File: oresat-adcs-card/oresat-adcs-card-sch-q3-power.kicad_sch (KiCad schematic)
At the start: 87 parts, among them Q31 MOSFET-PCH-SOT23-6, Q32 MOSFET-PCH-SOT23-6, Q33 PMV45EN2R, Q34 PMV45EN2R, Q35 MOSFET-PCH-dual-SOT23-6, U25 MAX7310ATE, U26 MAX4211FETE, U27 MIC842LYC5-TR, U28 MIC842LYC5-TR, U35 LTC3624, U37 TS5A21366DCUR

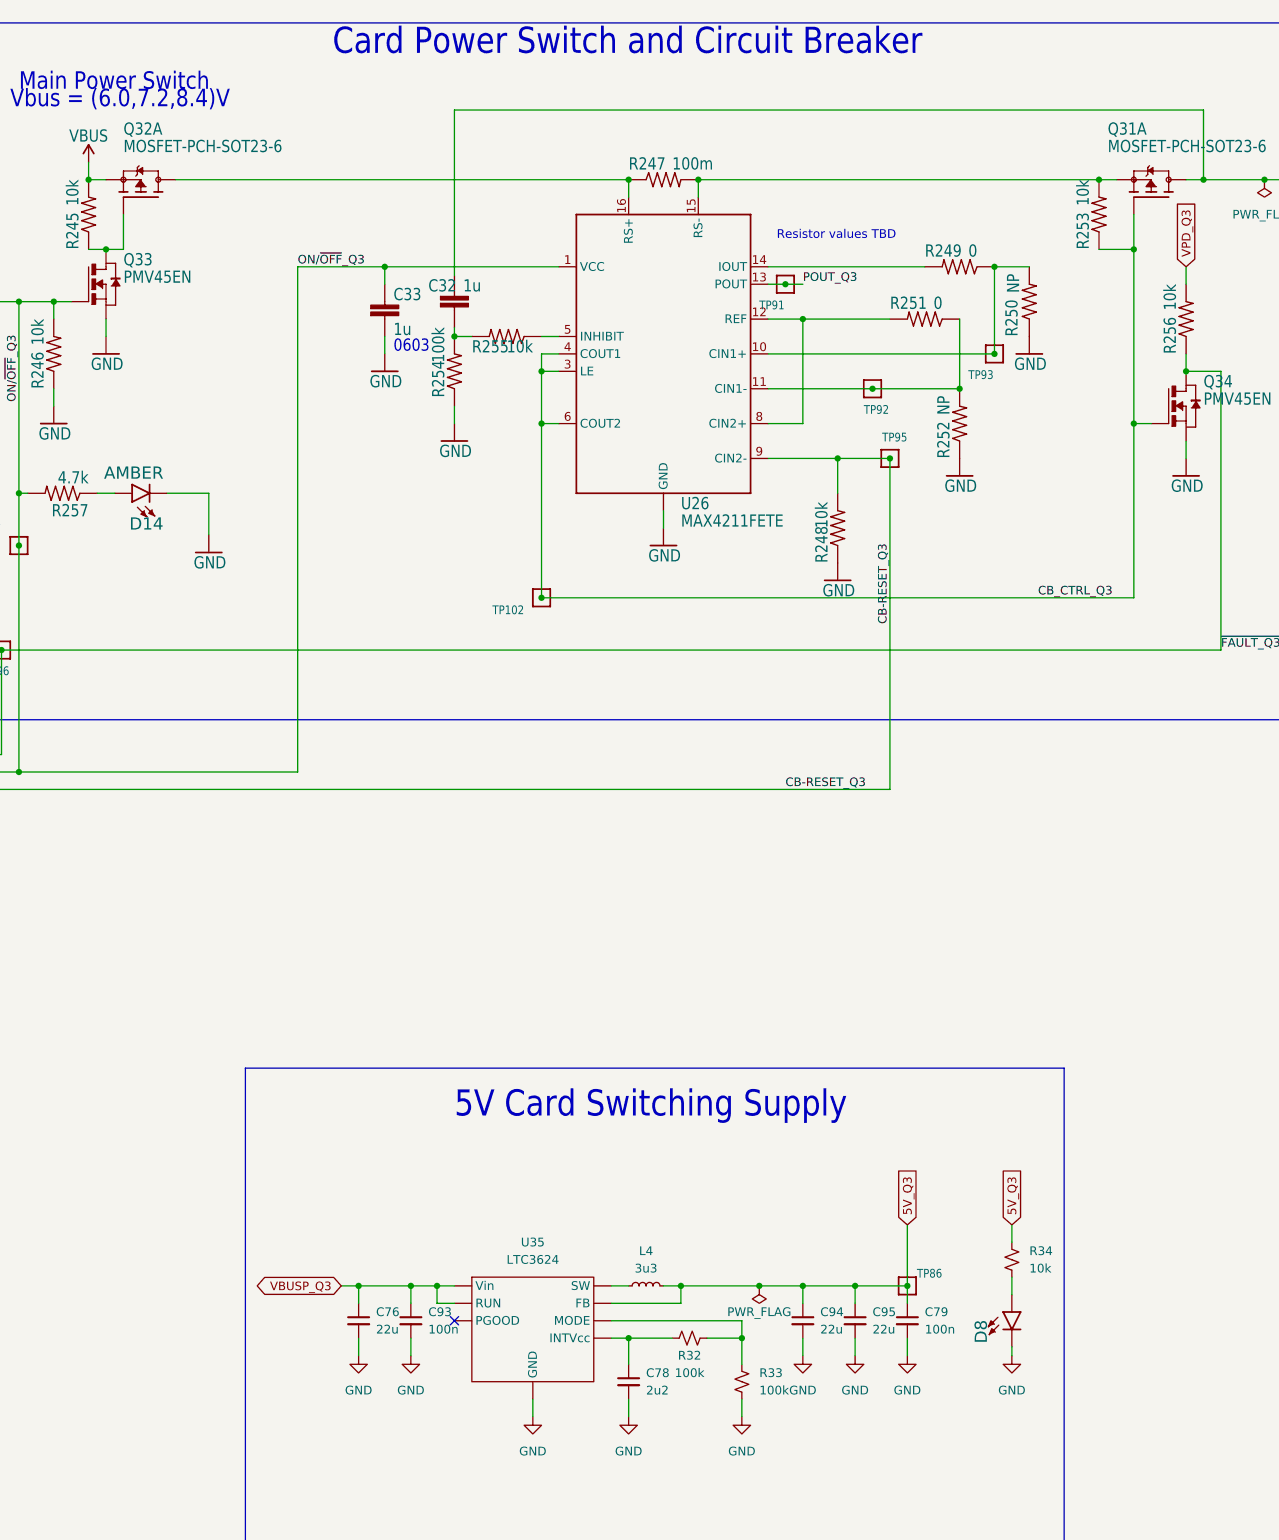
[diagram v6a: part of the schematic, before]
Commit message: Updated ADCS card and fixed library issues
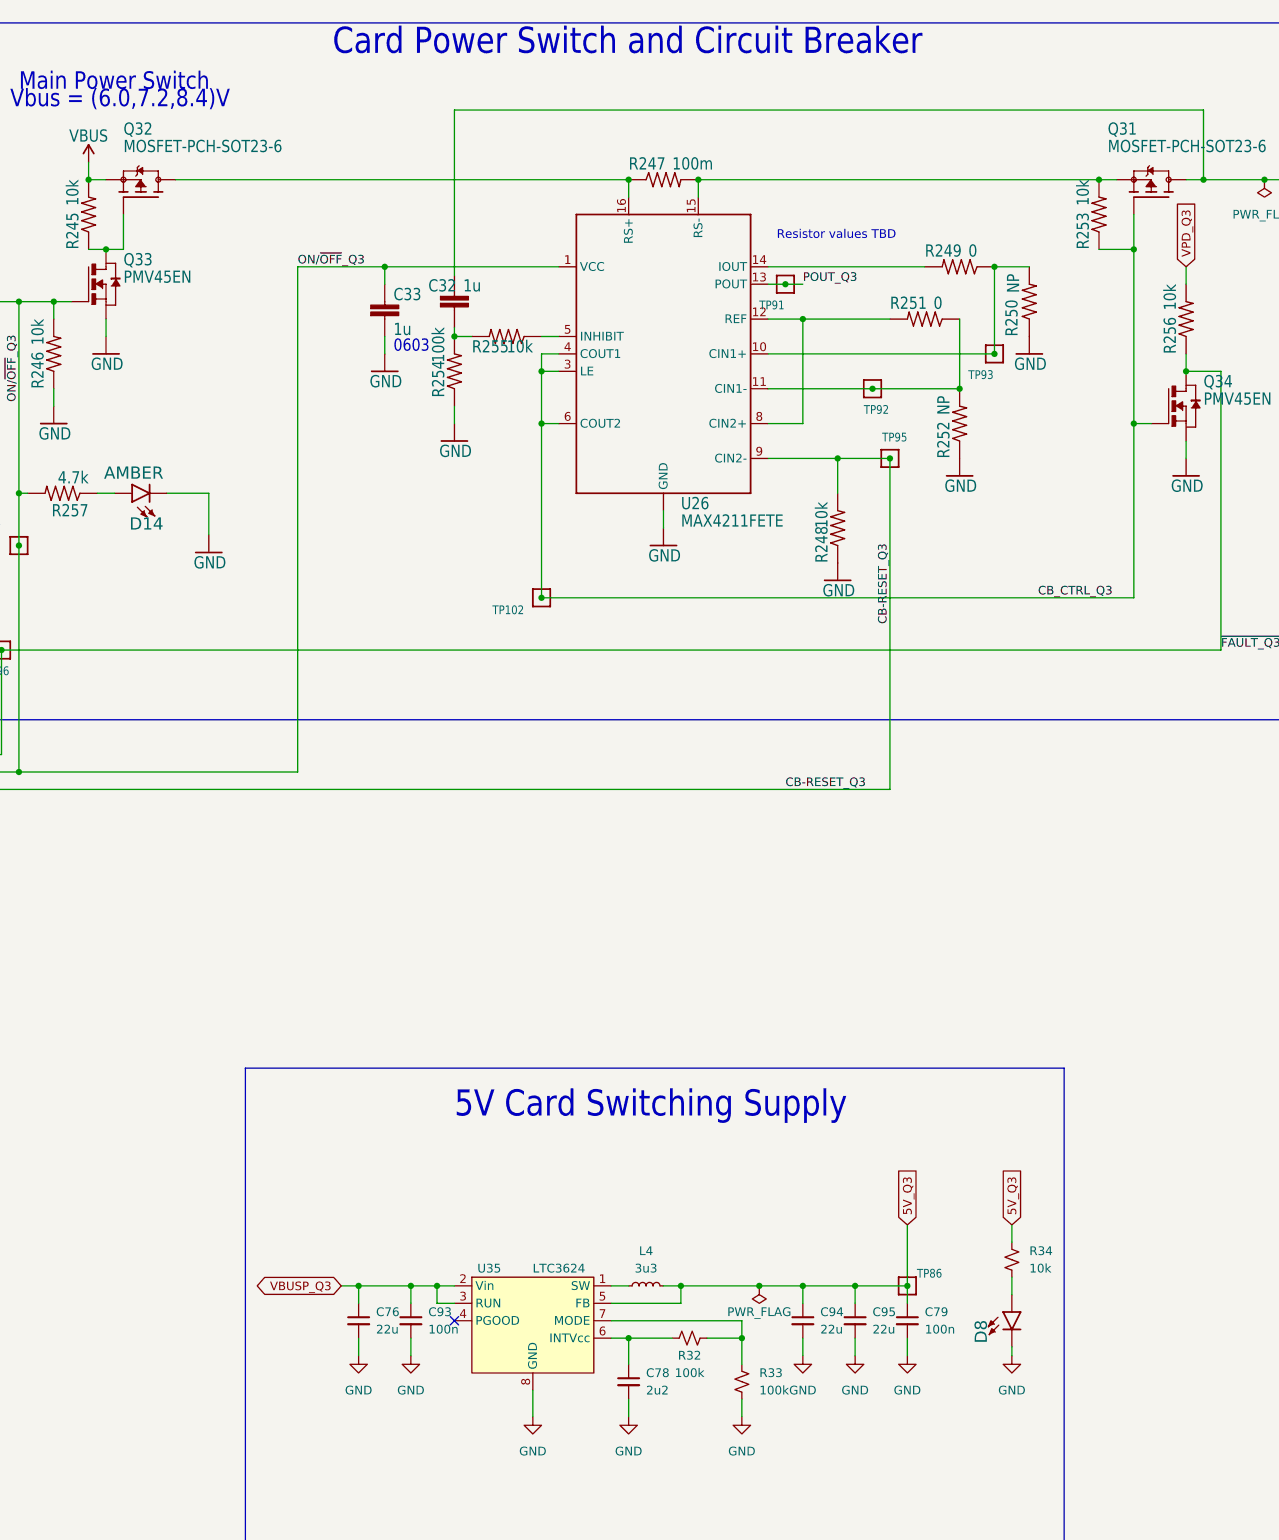
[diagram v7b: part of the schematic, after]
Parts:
- C31, C32, C33, C34, C35, C83, R115, R127, R229, R230, R231, R232, R233, R234, R235, R236, R237, R238, R239, R240, R241, R242, R243, R244, R245, R246, R248, R249, R250, R251, R252, R253, R254, R255, R256, R257, R258, R259, R260, R261, R262, R263, R264, R265, R266, R38: footprint oresat-acs-card:.0603-C-NOSILK -> oresat-passives:0603-C-NOSILK
- L4: footprint oresat-footprints:L_ECS-MPI4040 -> oresat-passives:L_ECS-MPI4040
- U35: footprint oresat-footprints:DFN-8-1EP_3x3mm_P0.5mm_EP1.65x2.38mm_ThermalVias0.3mm -> oresat-ics:DFN-8-1EP_3x3mm_P0.5mm_EP1.65x2.38mm_ThermalVias0.3mm; symbol U-Linear Tech-LTC3624:LTC3624 -> oresat-ics:LTC3624

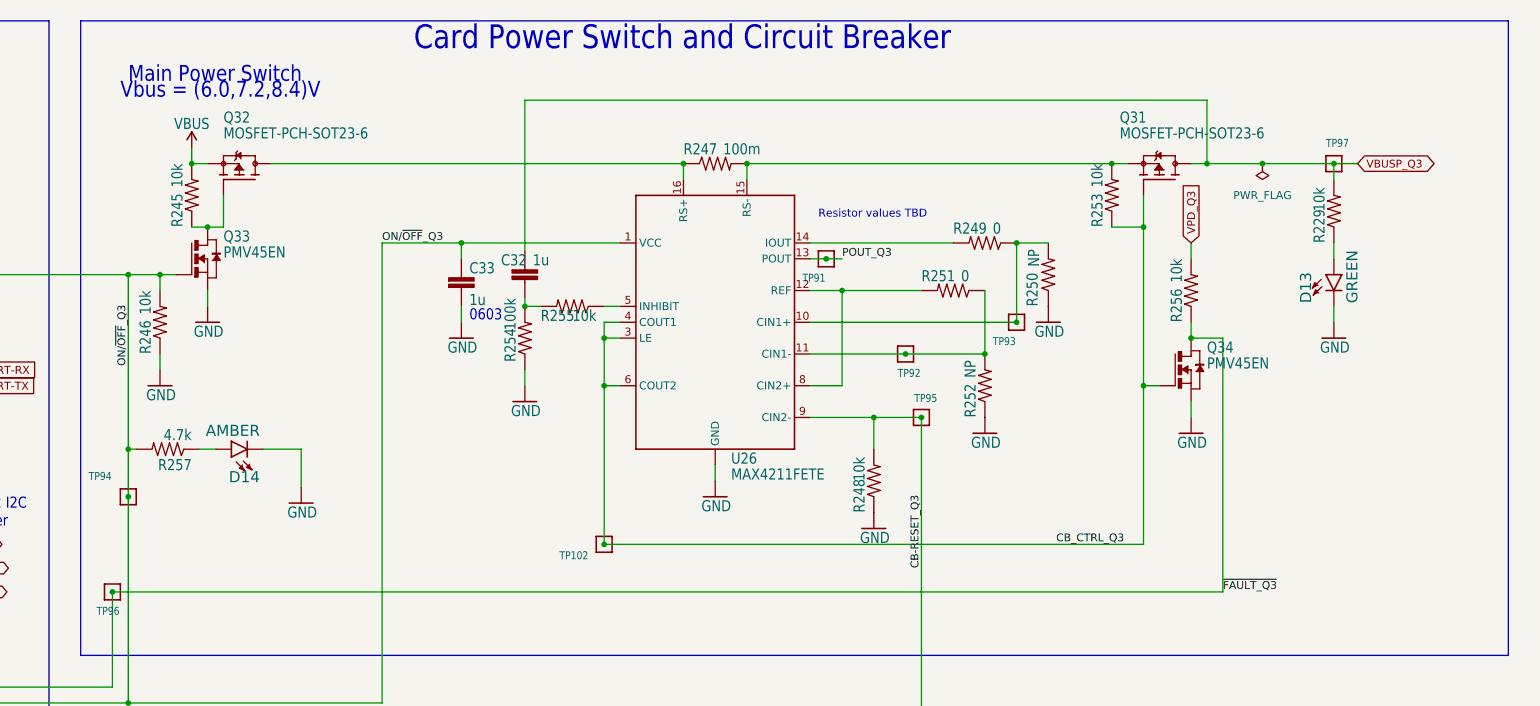
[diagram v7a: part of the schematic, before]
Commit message: Updated ADCS card, added soft-start to RW OPDs and updated current limits
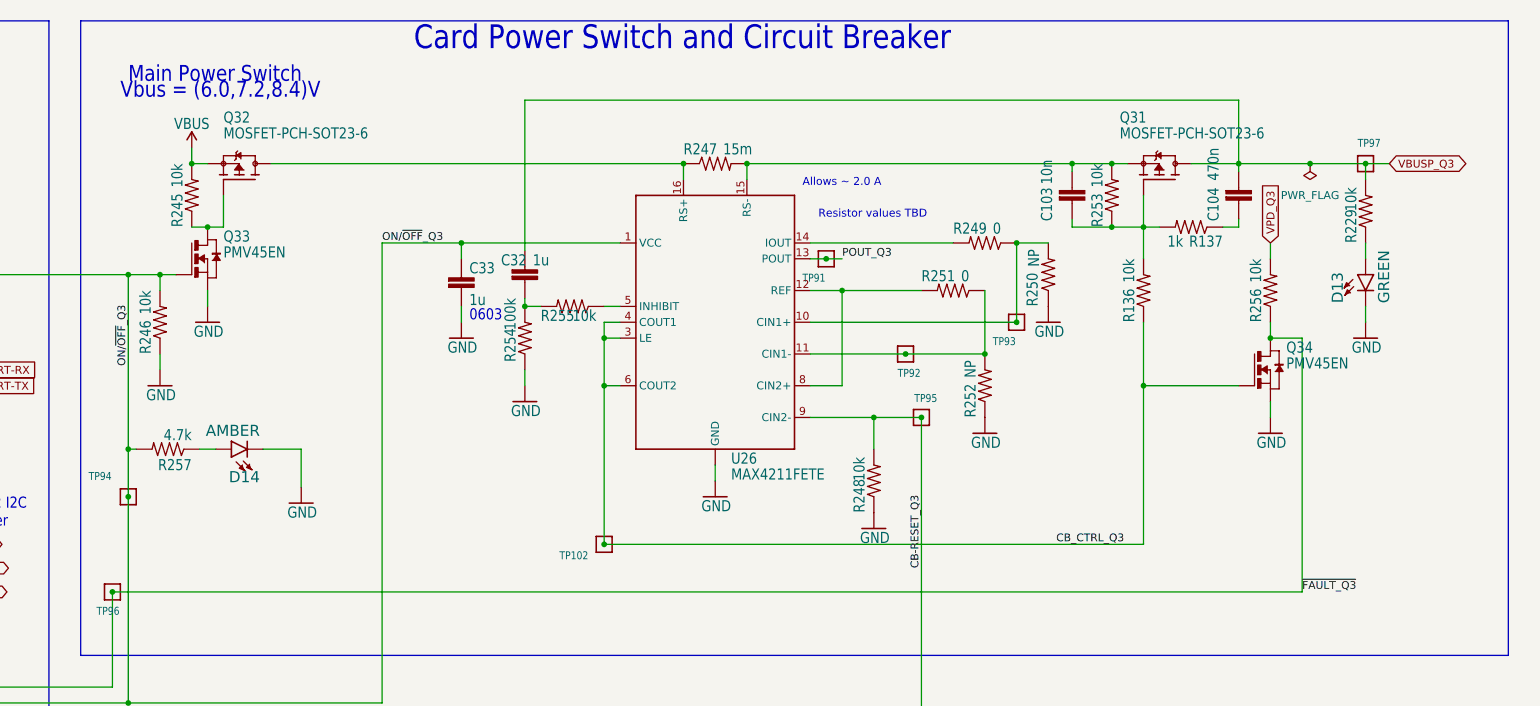
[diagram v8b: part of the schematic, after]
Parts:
- added C103: 10n, oresat-passives:0603-C-NOSILK, symbol oresat-acs-card-eagle-import:C-EU0603-C-NOSILK
- added C104: 470n, oresat-passives:0603-C-NOSILK, symbol oresat-acs-card-eagle-import:C-EU0603-C-NOSILK
- added R136, R137: RC0603FR-0710KL, oresat-passives:0603-C-NOSILK, symbol oresat-acs-card-eagle-import:R-US_0603-C-NOSILK
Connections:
- net CB_CTRL_Q3: now also R136.1; no longer Q31.3 (G), R253.1
- net VBUSP_Q3: now also C104.2
- net at Q31.4 (S), R247.2, R253.2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: now also C103.2
- new net: C103.1, Q31.3 (G), R136.2, R137.2, R253.1
- new net: C104.1, R137.1
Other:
- note added: "Allows ~ 2.0 A"
- moved on the sheet: D13, Q34, R229, R256, TP97
